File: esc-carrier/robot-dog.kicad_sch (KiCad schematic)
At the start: 35 parts, among them J1 Conn_01x02, J10 Conn_01x02, J11 Conn_01x04, J12 Conn_01x04, J13 Conn_01x04, J2 Conn_01x04, J3 Conn_01x04, J4 Conn_01x03, J5 Conn_01x05, J6 Conn_01x05, J7 Conn_01x05, J8 Conn_01x02, J9 Conn_01x02, SW1 SW_DIP_x02

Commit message: rearrange layout
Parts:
- J2, J3: footprint DogESCCarrier:Converter -> DogESCCarrier:VoltageConverter1
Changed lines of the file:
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@@
     (property "Reference" "J2" (id 0) (at 157.48 33.02 90))
     (property "Value" "Conn_01x04" (id 1) (at 157.48 35.56 90))
-    (property "Footprint" "DogESCCarrier:Converter" (id 2) (at 156.21 39.37 0)
+    (property "Footprint" "DogESCCarrier:VoltageConverter1" (id 2) (at 156.21 39.37 0)
       (effects (font (size 1.27 1.27)) hide)
     )
@@
     (property "Reference" "J3" (id 0) (at 177.8 33.02 90))
     (property "Value" "Conn_01x04" (id 1) (at 177.8 35.56 90))
-    (property "Footprint" "DogESCCarrier:Converter" (id 2) (at 176.53 39.37 0)
+    (property "Footprint" "DogESCCarrier:VoltageConverter1" (id 2) (at 176.53 39.37 0)
       (effects (font (size 1.27 1.27)) hide)
     )
@@
     )
     (path "/53116ff1-1454-4333-af0f-ed6e89f37d86"
-      (reference "J2") (unit 1) (value "Conn_01x04") (footprint "DogESCCarrier:Converter")
+      (reference "J2") (unit 1) (value "Conn_01x04") (footprint "DogESCCarrier:VoltageConverter1")
     )
     (path "/6c7d5f3f-36e7-4beb-b31c-94967dd0ddb5"
-      (reference "J3") (unit 1) (value "Conn_01x04") (footprint "DogESCCarrier:Converter")
+      (reference "J3") (unit 1) (value "Conn_01x04") (footprint "DogESCCarrier:VoltageConverter1")
     )
     (path "/b23cbf9a-af95-4260-8771-5f5618ec4148"

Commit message: adjust control board pos
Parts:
- J2, J3: footprint DogESCCarrier:VoltageConverter1 -> Connector_PinHeader_2.54mm:PinHeader_1x04_P2.54mm_Vertical
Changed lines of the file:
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@@
     (property "Reference" "J2" (id 0) (at 157.48 33.02 90))
     (property "Value" "Conn_01x04" (id 1) (at 157.48 35.56 90))
-    (property "Footprint" "DogESCCarrier:VoltageConverter1" (id 2) (at 156.21 39.37 0)
+    (property "Footprint" "Connector_PinHeader_2.54mm:PinHeader_1x04_P2.54mm_Vertical" (id 2) (at 156.21 39.37 0)
       (effects (font (size 1.27 1.27)) hide)
     )
@@
     (property "Reference" "J3" (id 0) (at 177.8 33.02 90))
     (property "Value" "Conn_01x04" (id 1) (at 177.8 35.56 90))
-    (property "Footprint" "DogESCCarrier:VoltageConverter1" (id 2) (at 176.53 39.37 0)
+    (property "Footprint" "Connector_PinHeader_2.54mm:PinHeader_1x04_P2.54mm_Vertical" (id 2) (at 176.53 39.37 0)
       (effects (font (size 1.27 1.27)) hide)
     )
@@
     )
     (path "/53116ff1-1454-4333-af0f-ed6e89f37d86"
-      (reference "J2") (unit 1) (value "Conn_01x04") (footprint "DogESCCarrier:VoltageConverter1")
+      (reference "J2") (unit 1) (value "Conn_01x04") (footprint "Connector_PinHeader_2.54mm:PinHeader_1x04_P2.54mm_Vertical")
     )
     (path "/6c7d5f3f-36e7-4beb-b31c-94967dd0ddb5"
-      (reference "J3") (unit 1) (value "Conn_01x04") (footprint "DogESCCarrier:VoltageConverter1")
+      (reference "J3") (unit 1) (value "Conn_01x04") (footprint "Connector_PinHeader_2.54mm:PinHeader_1x04_P2.54mm_Vertical")
     )
     (path "/b23cbf9a-af95-4260-8771-5f5618ec4148"

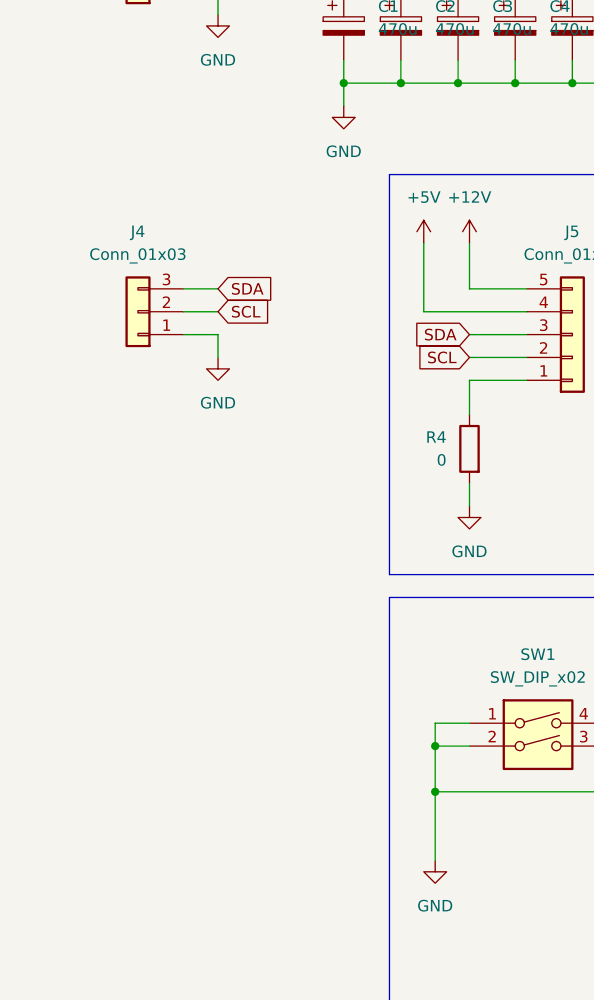
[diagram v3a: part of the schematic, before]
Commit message: add optional i2c pullups
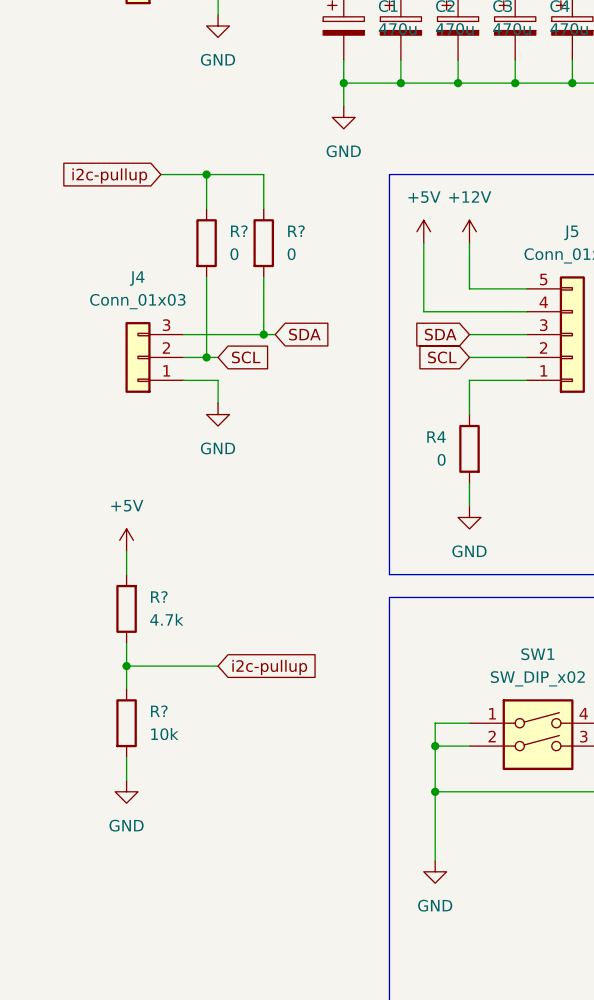
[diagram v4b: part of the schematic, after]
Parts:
- added R?: 10k, symbol Device:R
- added R?: 4.7k, symbol Device:R
- added R? (x2): 0, symbol Device:R
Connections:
- net +5V: now also R?.2
- net GND: now also R?.2
- net SCL: now also R?.2
- net SDA: now also R?.2
- new net i2c-pullup: R?.1, R?.1, R?.1, R?.1
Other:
- moved on the sheet: J4

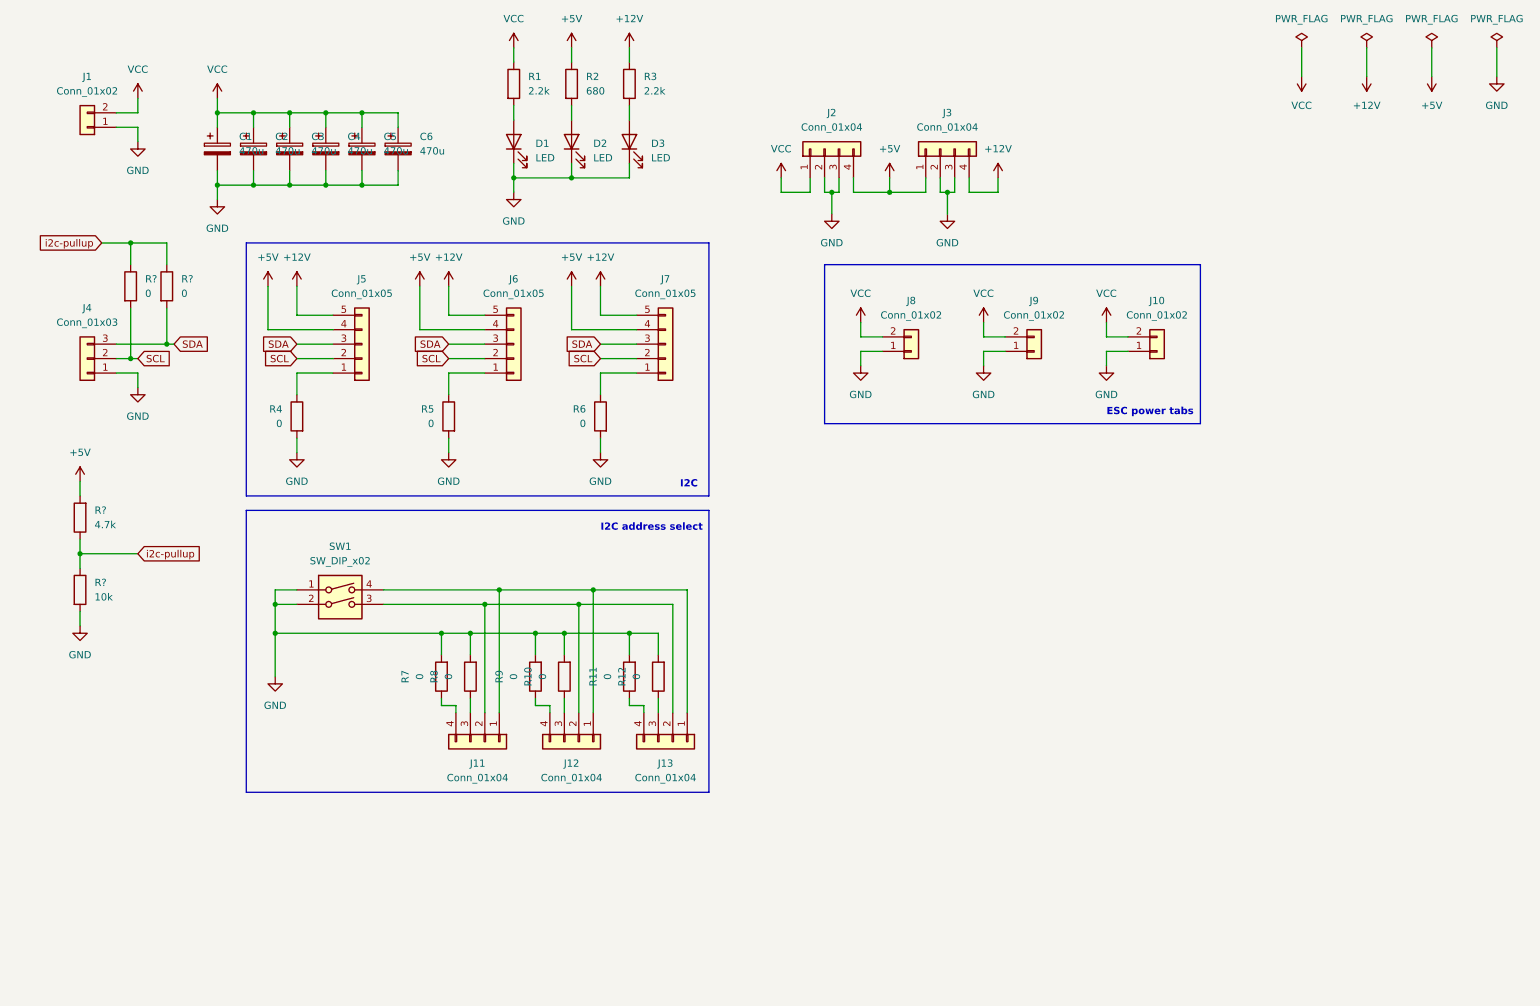
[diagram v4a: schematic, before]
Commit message: move i2c lines
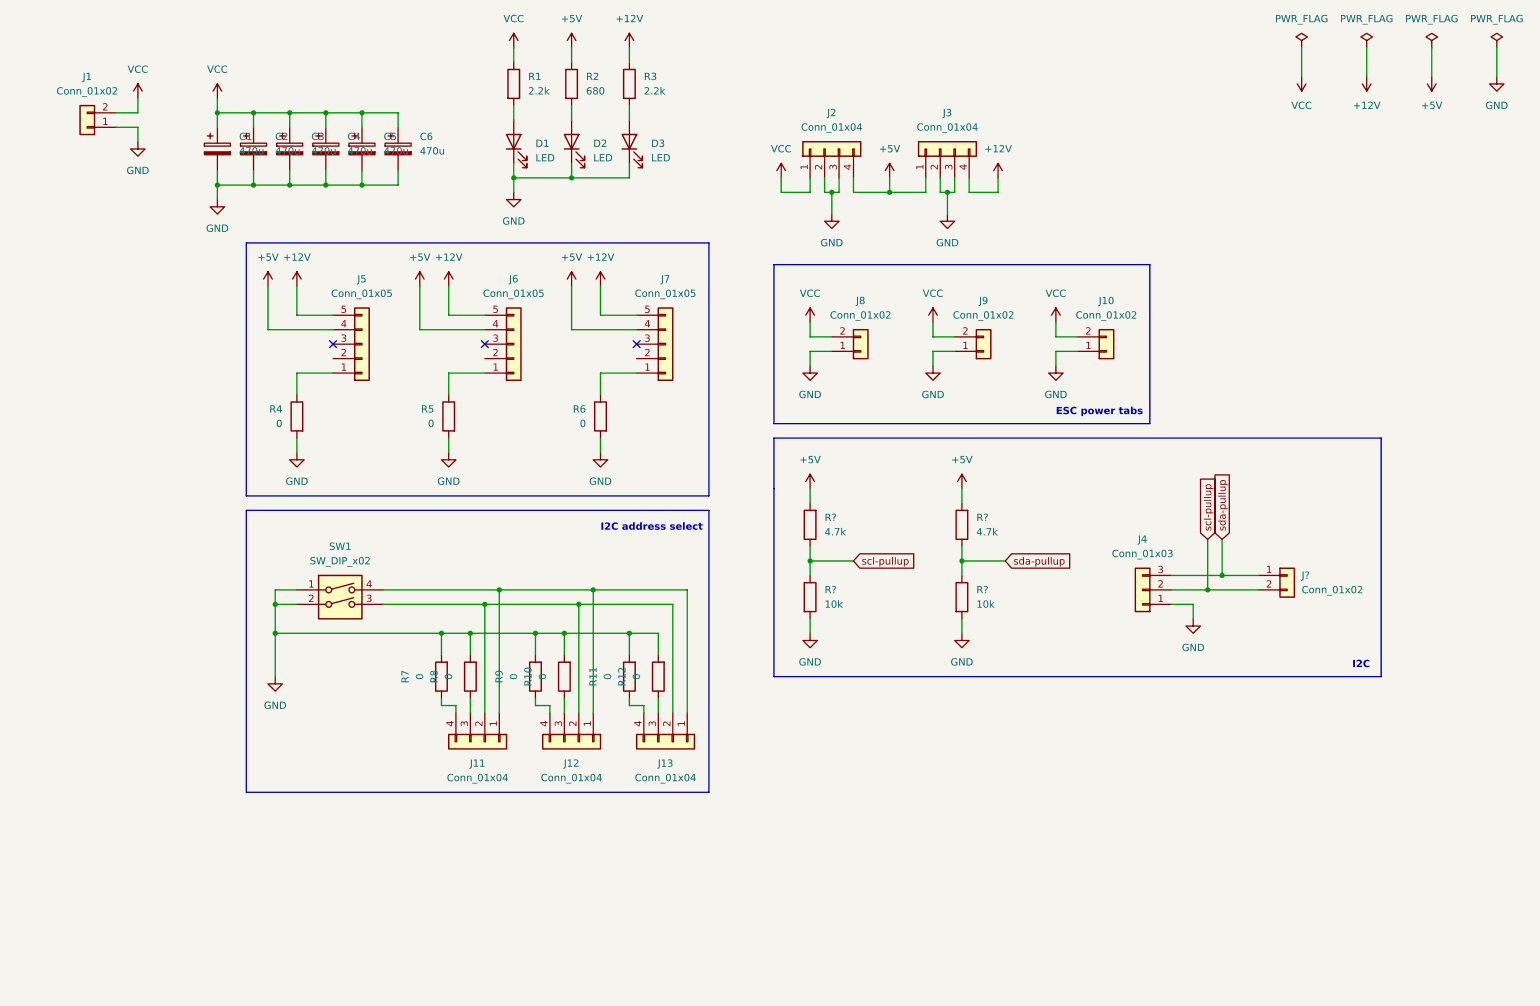
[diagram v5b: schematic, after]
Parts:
- removed R? (x2): 0, symbol Device:R
- added J?: Conn_01x02, symbol Connector_Generic:Conn_01x02
- added R?: 4.7k, symbol Device:R
- added R?: 10k, symbol Device:R
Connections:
- net +5V: now also R?.2
- net GND: now also R?.2
- removed net SCL: J4.2 (Pin_2), J5.2 (Pin_2), J6.2 (Pin_2), J7.2 (Pin_2)
- removed net SDA: J4.3 (Pin_3), J5.3 (Pin_3), J6.3 (Pin_3), J7.3 (Pin_3)
- net i2c-pullup renamed sda-pullup
- net sda-pullup: now also J4.3 (Pin_3), J?.1 (Pin_1)
- new net scl-pullup: J4.2 (Pin_2), J?.2 (Pin_2), R?.1, R?.1
- no-connect marks 0 -> 3
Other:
- moved on the sheet: J10, J4, J8, J9, R?

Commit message: add debugging points
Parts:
- added J? (x3): Conn_01x02, symbol Connector_Generic:Conn_01x02
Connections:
- net PGD-0: now reaches J11.4 (Pin_4), R7.1
- net PGD-0: now also J?.2 (Pin_2)
- net PGD-1: now reaches J12.4 (Pin_4), R9.1
- net PGD-1: now also J?.2 (Pin_2)
- net PGC-1: now reaches J6.2 (Pin_2)
- net PGC-1: now also J?.1 (Pin_1)
- net PGC-2: now reaches J7.2 (Pin_2)
- net PGC-2: now also J?.1 (Pin_1)
- net PGD-2: now reaches J13.4 (Pin_4), R11.1
- net PGD-2: now also J?.2 (Pin_2)
- net PGC-0: now reaches J5.2 (Pin_2)
- net PGC-0: now also J?.1 (Pin_1)
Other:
- note added: "Debugging"

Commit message: update PCB layout for i2c pullup/pin change and debugging pins
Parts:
- J10, J15, J16, J17: renamed from J?; footprint (none) -> Connector_PinHeader_2.54mm:PinHeader_1x02_P2.54mm_Vertical
- R10, R7, R8, R9: renamed from R?; footprint (none) -> Resistor_SMD:R_0603_1608Metric_Pad0.98x0.95mm_HandSolder
- renumbered J4 to J11, J11 to J12, J12 to J13, J13 to J14, J5 to J4, J6 to J5, J7 to J6, J8 to J7, J9 to J8, J10 to J9, R7 to R11, R8 to R12, R9 to R13, R10 to R14, R11 to R15, R12 to R16
